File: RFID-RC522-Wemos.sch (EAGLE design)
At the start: 18 parts, among them CON1 LCD, J4 VIN

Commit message: added missing values
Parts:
- BOARD1: value (none) -> 8x10
- C1: device SPCoast:CAP-POLPTH-5MM -> SPCoast:CAP-POL0810
- LED1, LED3: value (none) -> G
- LED2, LED4: value (none) -> R
- R1, R2: value (none) -> 1K0
- U$1: value (none) -> mini
- U$3: value (none) -> LCD
- VR: value (none) -> 5v
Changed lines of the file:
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@@
 <?xml version="1.0" encoding="utf-8"?>
 <!DOCTYPE eagle SYSTEM "eagle.dtd">
-<eagle version="7.6.0">
+<eagle version="7.7.0">
 <drawing>
 <settings>
@@
 <setting verticaltext="up"/>
 </settings>
-<grid distance="0.1" unitdist="inch" unit="inch" style="lines" multiple="1" display="no" altdistance="0.01" altunitdist="inch" altunit="inch"/>
+<grid distance="100" unitdist="mil" unit="mil" style="dots" multiple="1" display="yes" altdistance="50" altunitdist="mil" altunit="mil"/>
 <layers>
 <layer number="1" name="Top" color="4" fill="1" visible="yes" active="no"/>
@@
 <layer number="14" name="Route14" color="1" fill="6" visible="yes" active="no"/>
 <layer number="15" name="Route15" color="4" fill="6" visible="yes" active="no"/>
-<layer number="16" name="Bottom" color="1" fill="1" visible="yes" active="no"/>
-<layer number="17" name="Pads" color="2" fill="1" visible="yes" active="no"/>
-<layer number="18" name="Vias" color="2" fill="1" visible="yes" active="no"/>
+<layer number="16" name="Bottom" color="2" fill="1" visible="yes" active="no"/>
+<layer number="17" name="Pads" color="23" fill="1" visible="yes" active="no"/>
+<layer number="18" name="Vias" color="29" fill="1" visible="yes" active="no"/>
 <layer number="19" name="Unrouted" color="6" fill="1" visible="yes" active="no"/>
 <layer number="20" name="Dimension" color="15" fill="1" visible="yes" active="no"/>
-<layer number="21" name="tPlace" color="7" fill="1" visible="yes" active="no"/>
-<layer number="22" name="bPlace" color="7" fill="1" visible="yes" active="no"/>
-<layer number="23" name="tOrigins" color="15" fill="1" visible="yes" active="no"/>
+<layer number="21" name="tPlace" color="19" fill="1" visible="yes" active="no"/>
+<layer number="22" name="bPlace" color="17" fill="1" visible="yes" active="no"/>
+<layer number="23" name="tOrigins" color="30" fill="1" visible="yes" active="no"/>
 <layer number="24" name="bOrigins" color="15" fill="1" visible="yes" active="no"/>
-<layer number="25" name="tNames" color="7" fill="1" visible="yes" active="no"/>
-<layer number="26" name="bNames" color="7" fill="1" visible="yes" active="no"/>
-<layer number="27" name="tValues" color="7" fill="1" visible="yes" active="no"/>
+<layer number="25" name="tNames" color="63" fill="1" visible="yes" active="no"/>
+<layer number="26" name="bNames" color="34" fill="1" visible="yes" active="no"/>
+<layer number="27" name="tValues" color="56" fill="1" visible="yes" active="no"/>
 <layer number="28" name="bValues" color="7" fill="1" visible="yes" active="no"/>
 <layer number="29" name="tStop" color="7" fill="3" visible="no" active="no"/>
@@
 <layer number="38" name="bTest" color="7" fill="1" visible="yes" active="no"/>
 <layer number="39" name="tKeepout" color="4" fill="11" visible="no" active="no"/>
-<layer number="40" name="bKeepout" color="1" fill="11" visible="no" active="no"/>
+<layer number="40" name="bKeepout" color="3" fill="11" visible="no" active="no"/>
 <layer number="41" name="tRestrict" color="4" fill="10" visible="no" active="no"/>
-<layer number="42" name="bRestrict" color="1" fill="10" visible="no" active="no"/>
+<layer number="42" name="bRestrict" color="3" fill="10" visible="no" active="no"/>
 <layer number="43" name="vRestrict" color="2" fill="10" visible="no" active="no"/>
-<layer number="44" name="Drills" color="7" fill="1" visible="no" active="no"/>
-<layer number="45" name="Holes" color="7" fill="1" visible="no" active="no"/>
-<layer number="46" name="Milling" color="3" fill="1" visible="yes" active="no"/>
-<layer number="47" name="Measures" color="7" fill="1" visible="yes" active="no"/>
-<layer number="48" name="Document" color="7" fill="1" visible="yes" active="no"/>
-<layer number="49" name="Reference" color="7" fill="1" visible="yes" active="no"/>
+<layer number="44" name="Drills" color="16" fill="1" visible="no" active="no"/>
+<layer number="45" name="Holes" color="35" fill="1" visible="no" active="no"/>
+<layer number="46" name="Milling" color="35" fill="1" visible="yes" active="no"/>
+<layer number="47" name="Measures" color="21" fill="1" visible="yes" active="no"/>
+<layer number="48" name="Document" color="24" fill="1" visible="yes" active="no"/>
+<layer number="49" name="Reference" color="48" fill="1" visible="yes" active="no"/>
 <layer number="50" name="dxf" color="7" fill="1" visible="yes" active="no"/>
-<layer number="51" name="tDocu" color="7" fill="1" visible="yes" active="no"/>
+<layer number="51" name="tDocu" color="24" fill="1" visible="yes" active="no"/>
 <layer number="52" name="bDocu" color="7" fill="1" visible="yes" active="no"/>
 <layer number="53" name="tGND_GNDA" color="7" fill="9" visible="yes" active="no"/>
@@
 <parts>
 <part name="FRAME1" library="SPCoast" deviceset="DOC-FRAME-LETTER" device=""/>
-<part name="U$1" library="SPCoast" deviceset="WEMOS-D1" device="V1"/>
+<part name="U$1" library="SPCoast" deviceset="WEMOS-D1" device="V1" value="mini"/>
 <part name="U$2" library="SPCoast" deviceset="RFID" device="BACK"/>
-<part name="U$3" library="SPCoast" deviceset="LCD" device="1602"/>
+<part name="U$3" library="SPCoast" deviceset="LCD" device="1602" value="LCD"/>
 <part name="CON1" library="SPCoast" deviceset="CONNECTOR-I2C" device="LEFT" value="LCD"/>
 <part name="+3V2" library="supply1" deviceset="+3V3" device=""/>
@@
 <part name="SUPPLY2" library="supply2" deviceset="+9V" device=""/>
 <part name="V12" library="supply2" deviceset="GND" device=""/>
-<part name="C1" library="SPCoast" deviceset="CAP-POL*" device="PTH-5MM" value="220uF"/>
+<part name="C1" library="SPCoast" deviceset="CAP-POL*" device="0810" value="220uF"/>
 <part name="J4" library="SPCoast" deviceset="CONNECTOR-DC-POWER" device="-RA" value="VIN"/>
 <part name="POWER" library="SPCoast" deviceset="DOC-POWER_LABEL" device="" value="9-12vDC"/>
 <part name="C3" library="SPCoast" deviceset="CAP*" device="0805" value=".1uF"/>
 <part name="C2" library="SPCoast" deviceset="CAP*" device="0805" value=".1uF"/>
-<part name="VR" library="SPCoast" deviceset="VREG_78XX" device="-1300040P1"/>
-<part name="BOARD1" library="SPCoast" deviceset="BOARD" device="80X100"/>
+<part name="VR" library="SPCoast" deviceset="VREG_78XX" device="-1300040P1" value="5v"/>
+<part name="BOARD1" library="SPCoast" deviceset="BOARD" device="80X100" value="8x10"/>
 <part name="P+1" library="supply1" deviceset="VCC" device=""/>
 <part name="P+2" library="supply1" deviceset="VCC" device=""/>
 <part name="P+3" library="supply1" deviceset="VCC" device=""/>
-<part name="R1" library="SPCoast" deviceset="R*" device="0805-RES"/>
-<part name="R2" library="SPCoast" deviceset="R*" device="0805-RES"/>
-<part name="LED1" library="SPCoast" deviceset="LED*" device="0603-LED"/>
-<part name="LED2" library="SPCoast" deviceset="LED*" device="0603-LED"/>
+<part name="R1" library="SPCoast" deviceset="R*" device="0805-RES" value="1K0"/>
+<part name="R2" library="SPCoast" deviceset="R*" device="0805-RES" value="1K0"/>
+<part name="LED1" library="SPCoast" deviceset="LED*" device="0603-LED" value="G"/>
+<part name="LED2" library="SPCoast" deviceset="LED*" device="0603-LED" value="R"/>
 <part name="GND4" library="supply1" deviceset="GND" device=""/>
 <part name="LOGO1" library="SPCoast" deviceset="DOC-OSHW-LOGO" device="L"/>
-<part name="LED3" library="SPCoast" deviceset="LED*" device="LED5MM"/>
-<part name="LED4" library="SPCoast" deviceset="LED*" device="LED5MM"/>
+<part name="LED3" library="SPCoast" deviceset="LED*" device="LED5MM" value="G"/>
+<part name="LED4" library="SPCoast" deviceset="LED*" device="LED5MM" value="R"/>
 </parts>
 <sheets>

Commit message: added missing values
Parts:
- C2: value .1uF -> 1uF
- C3: value .1uF -> 10uF
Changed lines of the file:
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@@
 <part name="J4" library="SPCoast" deviceset="CONNECTOR-DC-POWER" device="-RA" value="VIN"/>
 <part name="POWER" library="SPCoast" deviceset="DOC-POWER_LABEL" device="" value="9-12vDC"/>
-<part name="C3" library="SPCoast" deviceset="CAP*" device="0805" value=".1uF"/>
-<part name="C2" library="SPCoast" deviceset="CAP*" device="0805" value=".1uF"/>
+<part name="C3" library="SPCoast" deviceset="CAP*" device="0805" value="10uF"/>
+<part name="C2" library="SPCoast" deviceset="CAP*" device="0805" value="1uF"/>
 <part name="VR" library="SPCoast" deviceset="VREG_78XX" device="-1300040P1" value="5v"/>
 <part name="BOARD1" library="SPCoast" deviceset="BOARD" device="80X100" value="8x10"/>

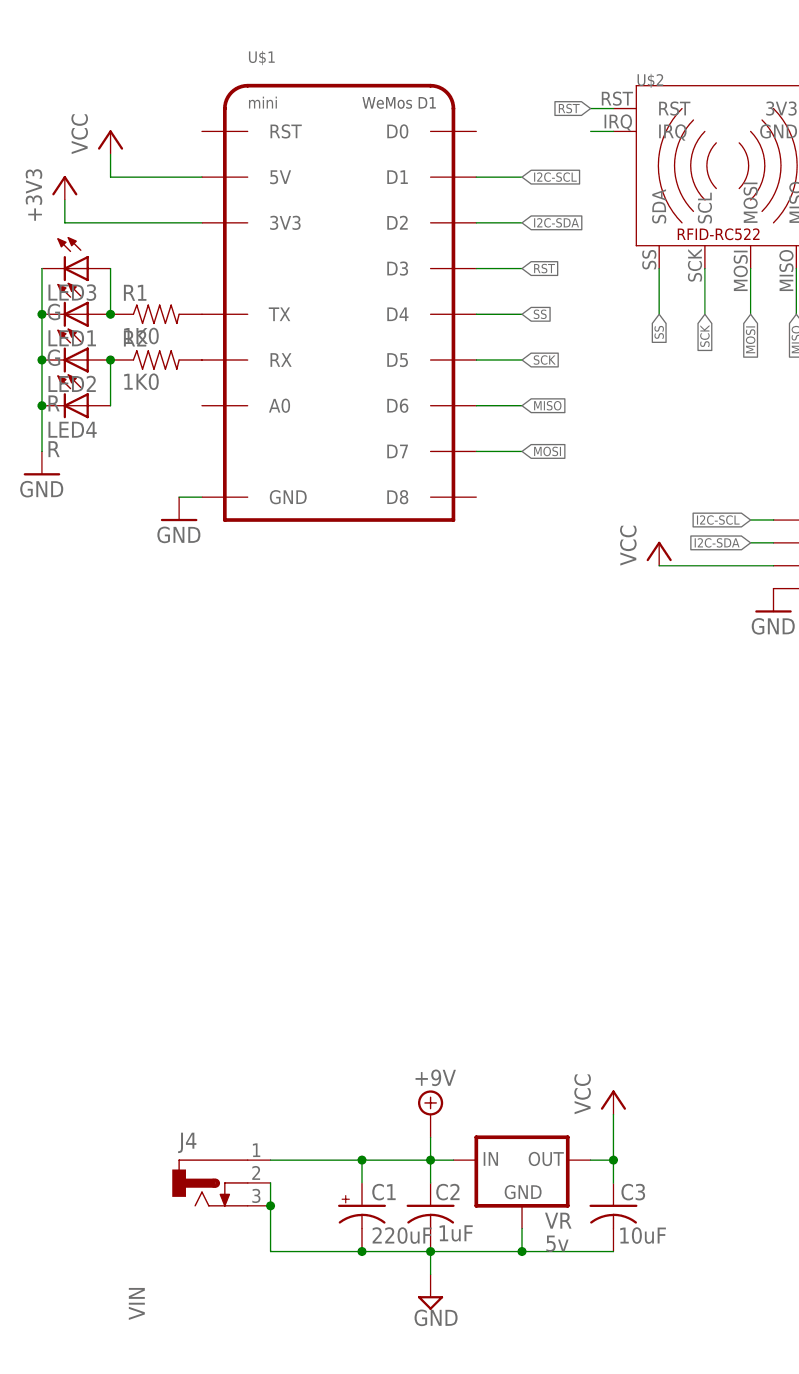
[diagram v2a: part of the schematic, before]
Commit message: normalized values
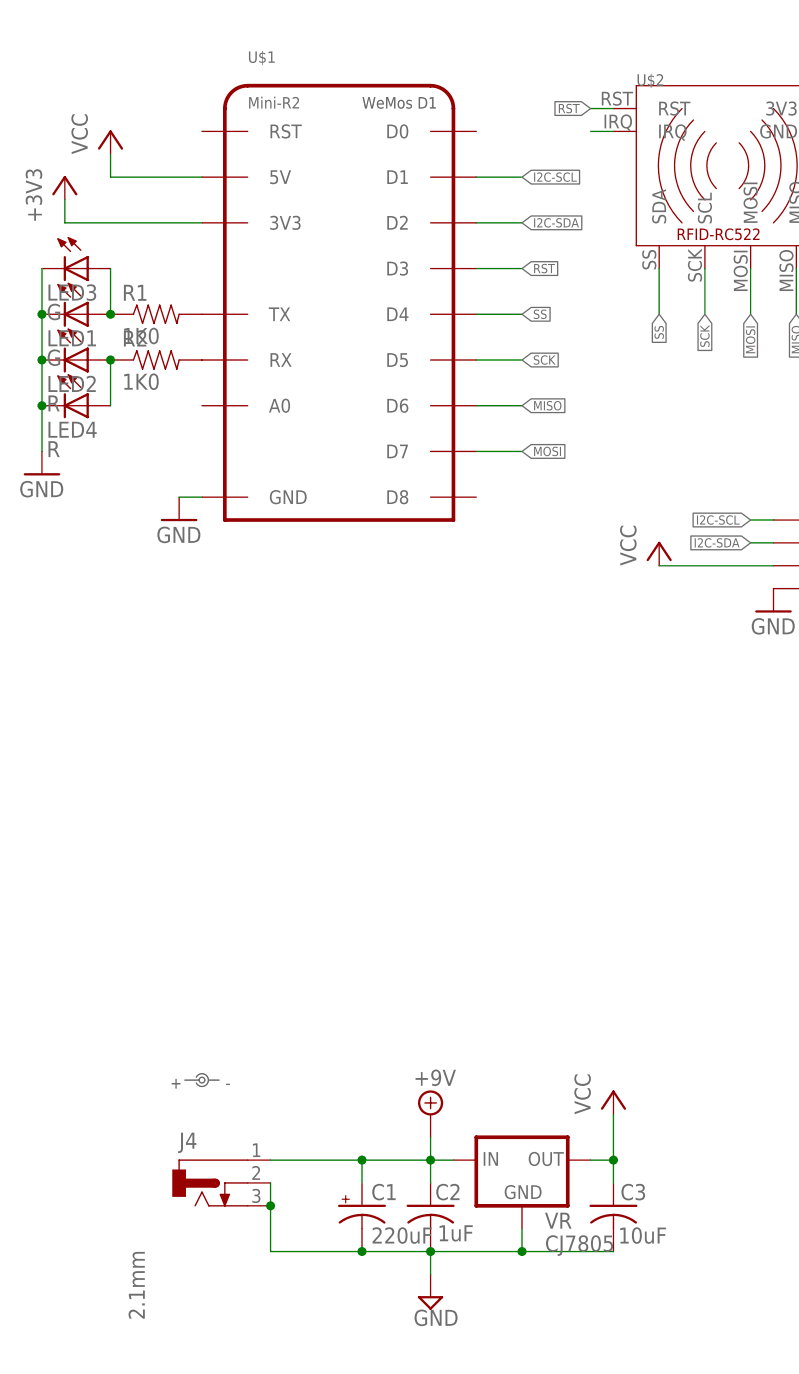
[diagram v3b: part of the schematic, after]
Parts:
- C2, C3: device SPCoast:CAP0805 -> SPCoast:CAP0603
- J4: value VIN -> 2.1mm
- LOGO1: value DOC-OSHW-LOGOL -> OSHW
- R2: device SPCoast:R0805-RES -> SPCoast:R0603-RES
- U$1: value mini -> Mini-R2
- VR: value 5v -> CJ7805; device SPCoast:VREG_78XX-1300040P1 -> SPCoast:VREG-DPAK-5
